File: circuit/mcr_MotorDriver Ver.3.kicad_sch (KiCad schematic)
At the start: 0 parts

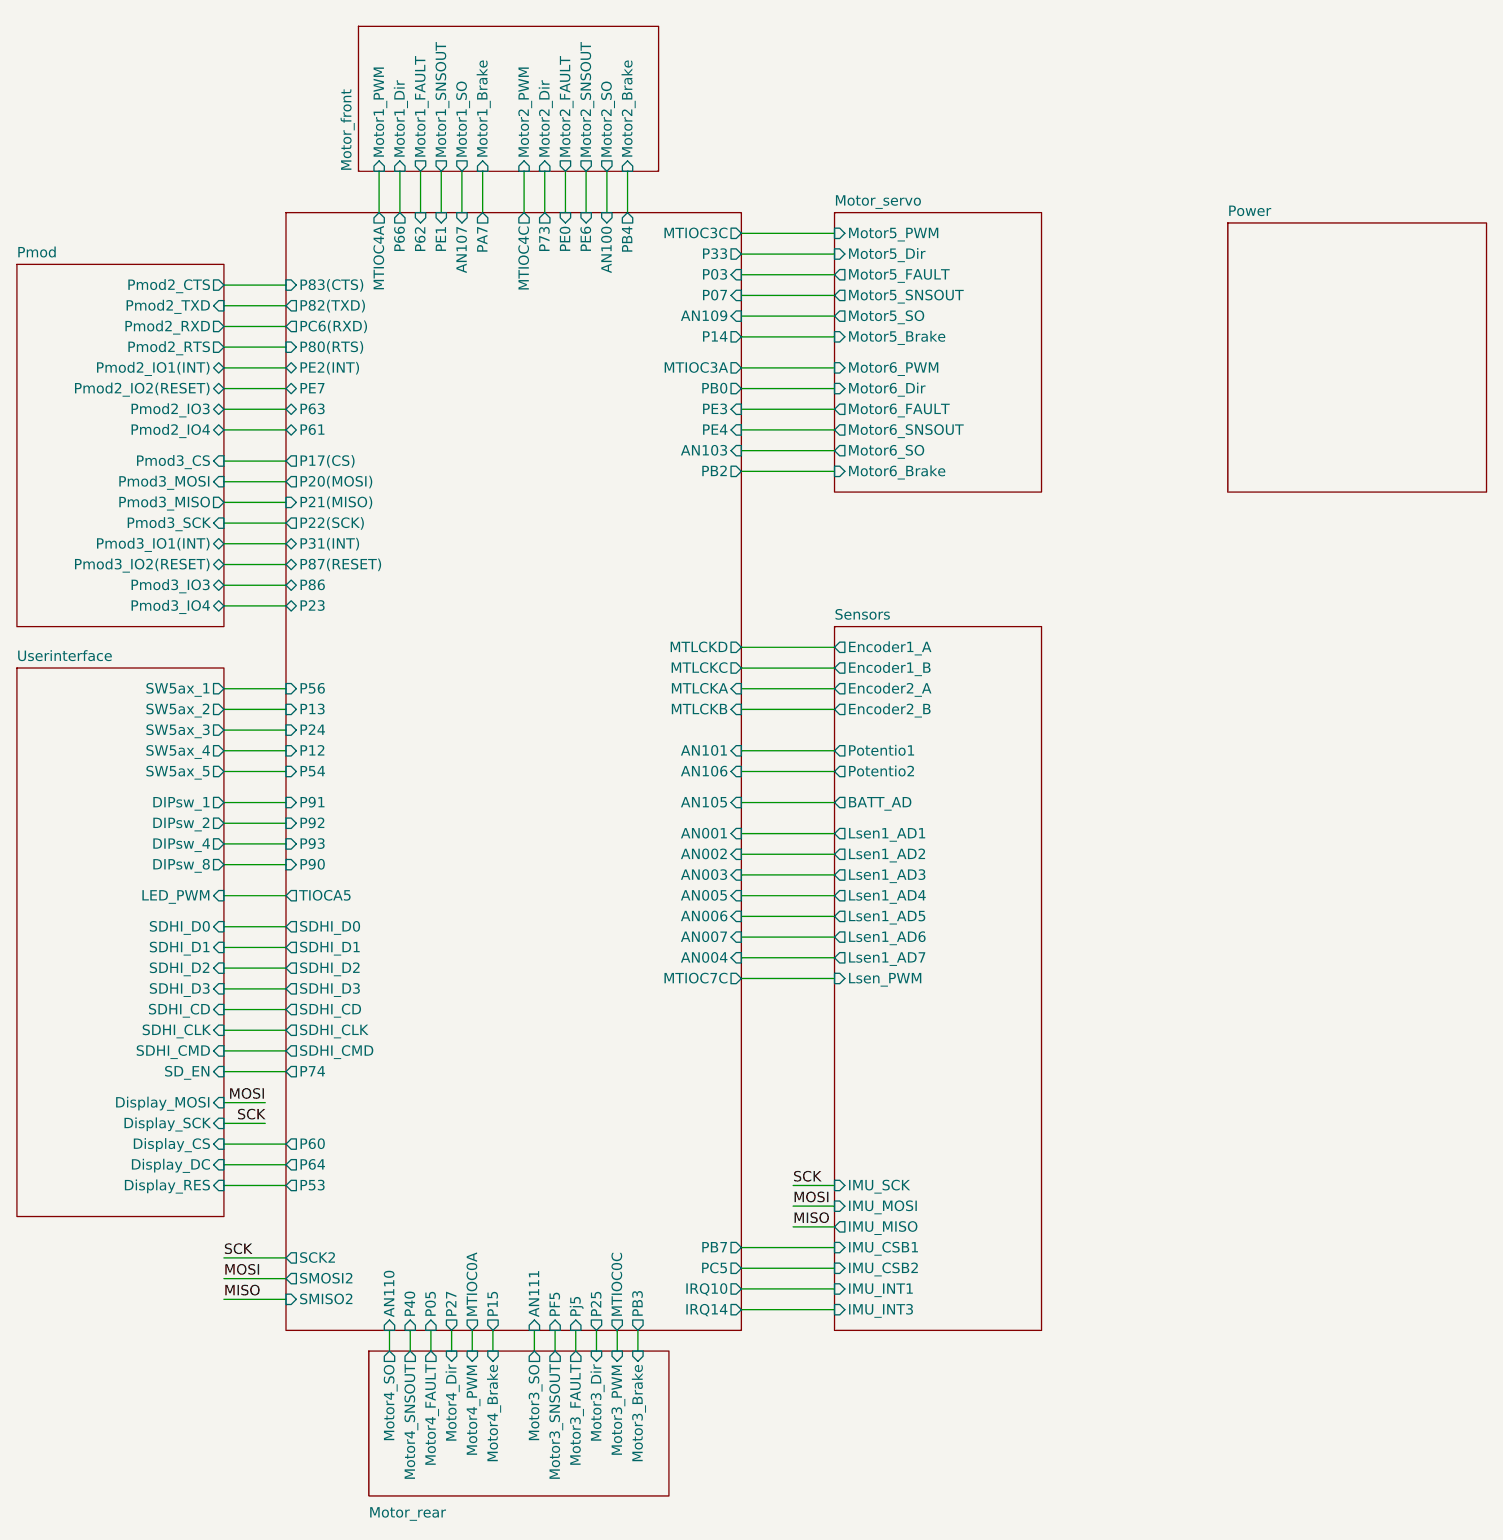
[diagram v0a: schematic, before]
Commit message: スマコンの設定変更 回路図変更
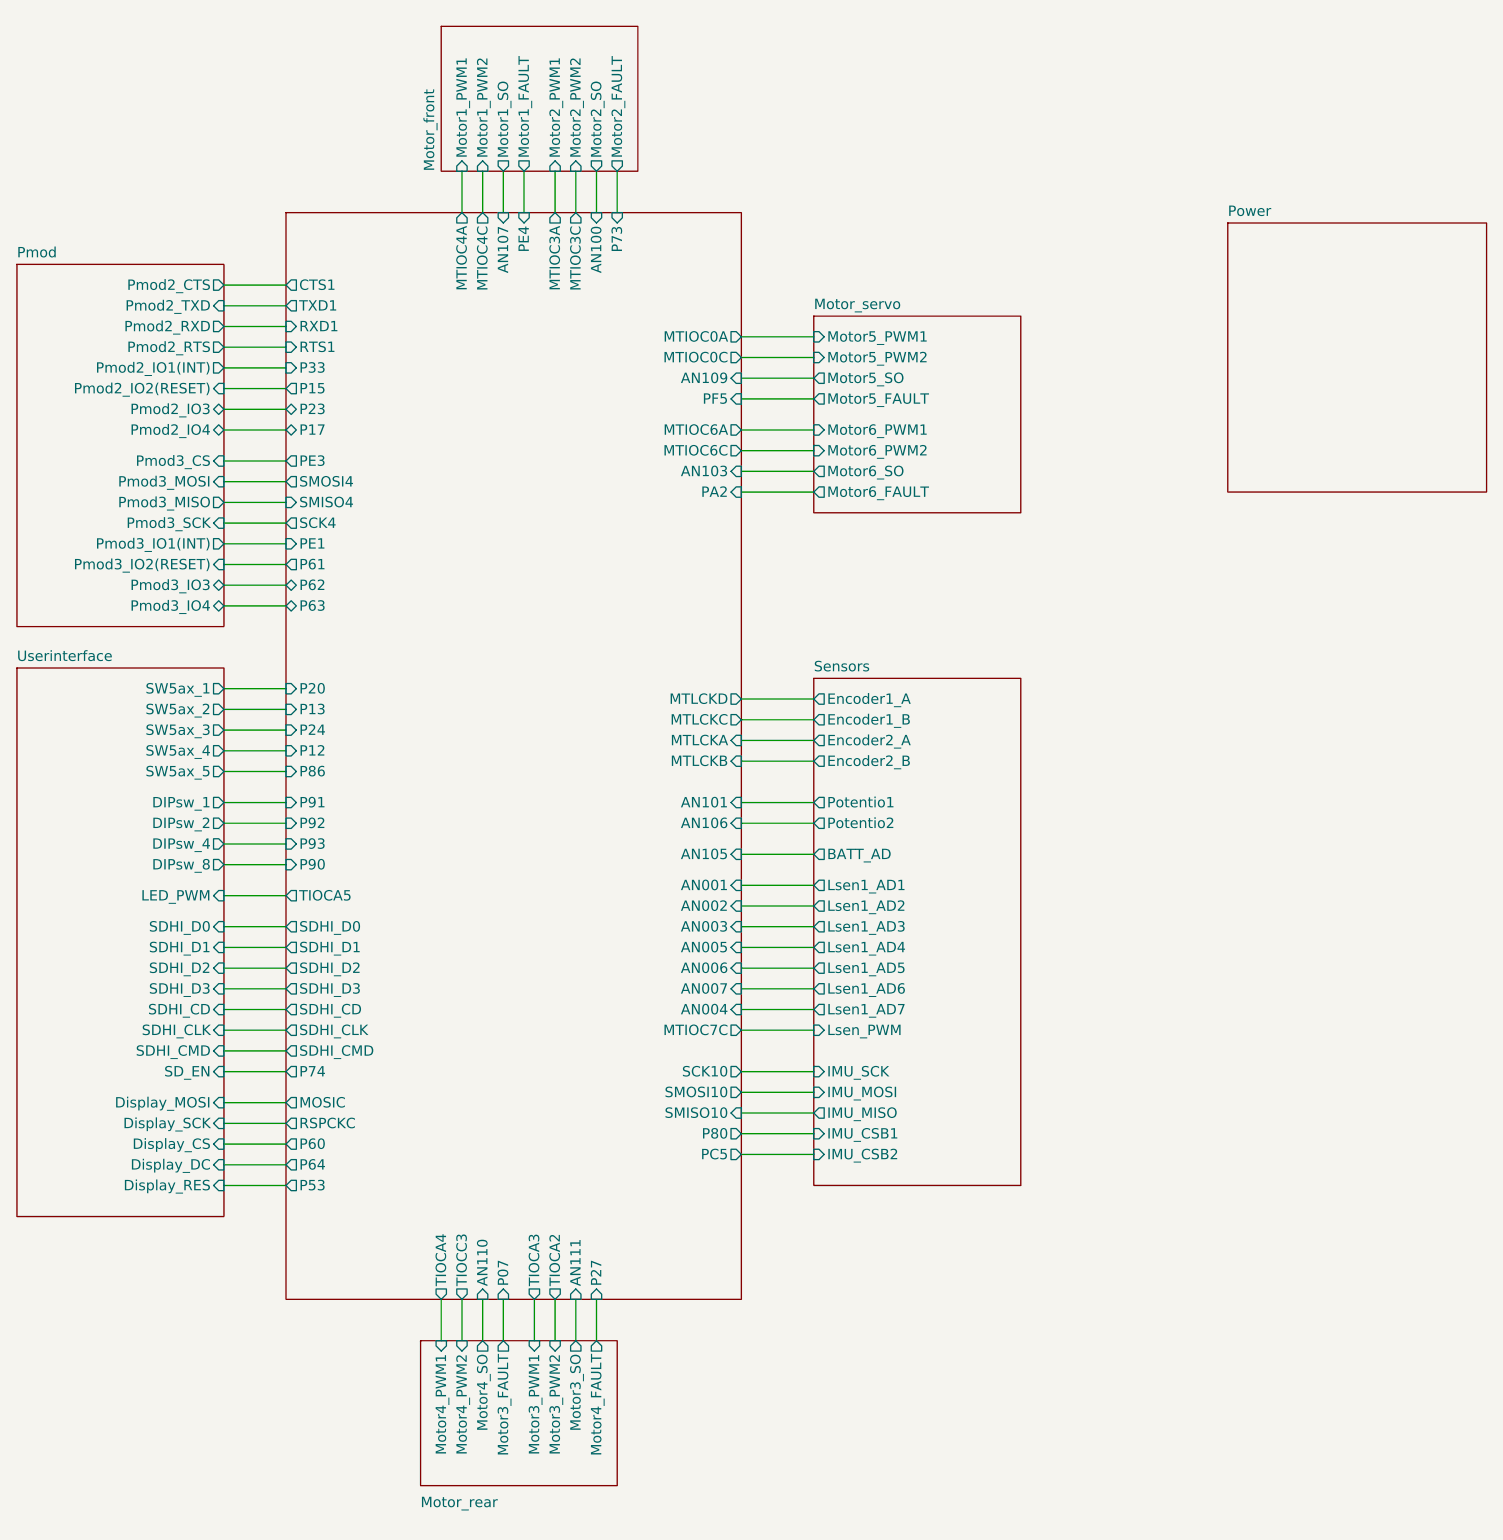
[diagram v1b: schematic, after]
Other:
- sheet MCU ports: added CTS1, MOSIC, MTIOC6A, MTIOC6C, P17, P20, P80, PA2, RSPCKC, RTS1, RXD1, SCK10, SCK4, SMISO10, SMISO4, SMOSI10, SMOSI4, TIOCA2, TIOCA3, TIOCA4, TIOCC3, TXD1; removed IRQ10, IRQ14, P03, P05, P14, P17(CS), P20(MOSI), P21(MISO), P22(SCK), P25, P31(INT), P40, P54, P56, P66, P80(RTS), P82(TXD), P83(CTS), P87(RESET), PA7, PB0, PB2, PB3, PB4, PB7, PC6(RXD), PE0, PE2(INT), PE6, PE7, Pj5, SCK2, SMISO2, SMOSI2
- sheet Motor_front ports: added Motor1_PWM1, Motor1_PWM2, Motor2_PWM1, Motor2_PWM2; removed Motor1_Brake, Motor1_Dir, Motor1_PWM, Motor1_SNSOUT, Motor2_Brake, Motor2_Dir, Motor2_PWM, Motor2_SNSOUT
- sheet Motor_rear ports: added Motor3_PWM1, Motor3_PWM2, Motor4_PWM1, Motor4_PWM2; removed Motor3_Brake, Motor3_Dir, Motor3_PWM, Motor3_SNSOUT, Motor4_Brake, Motor4_Dir, Motor4_PWM, Motor4_SNSOUT
- sheet Motor_servo ports: added Motor5_PWM1, Motor5_PWM2, Motor6_PWM1, Motor6_PWM2; removed Motor5_Brake, Motor5_Dir, Motor5_PWM, Motor5_SNSOUT, Motor6_Brake, Motor6_Dir, Motor6_PWM, Motor6_SNSOUT
- sheet Sensors ports: added none; removed IMU_INT1, IMU_INT3
